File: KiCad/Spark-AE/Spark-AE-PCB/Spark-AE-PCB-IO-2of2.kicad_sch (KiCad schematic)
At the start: 42 parts, among them J7 SD_CONN, U6 MCP6002T-I_MS, U8 MCP6002T-I_MS, U9 74xGxx_MDD_74AHCT1G125GV

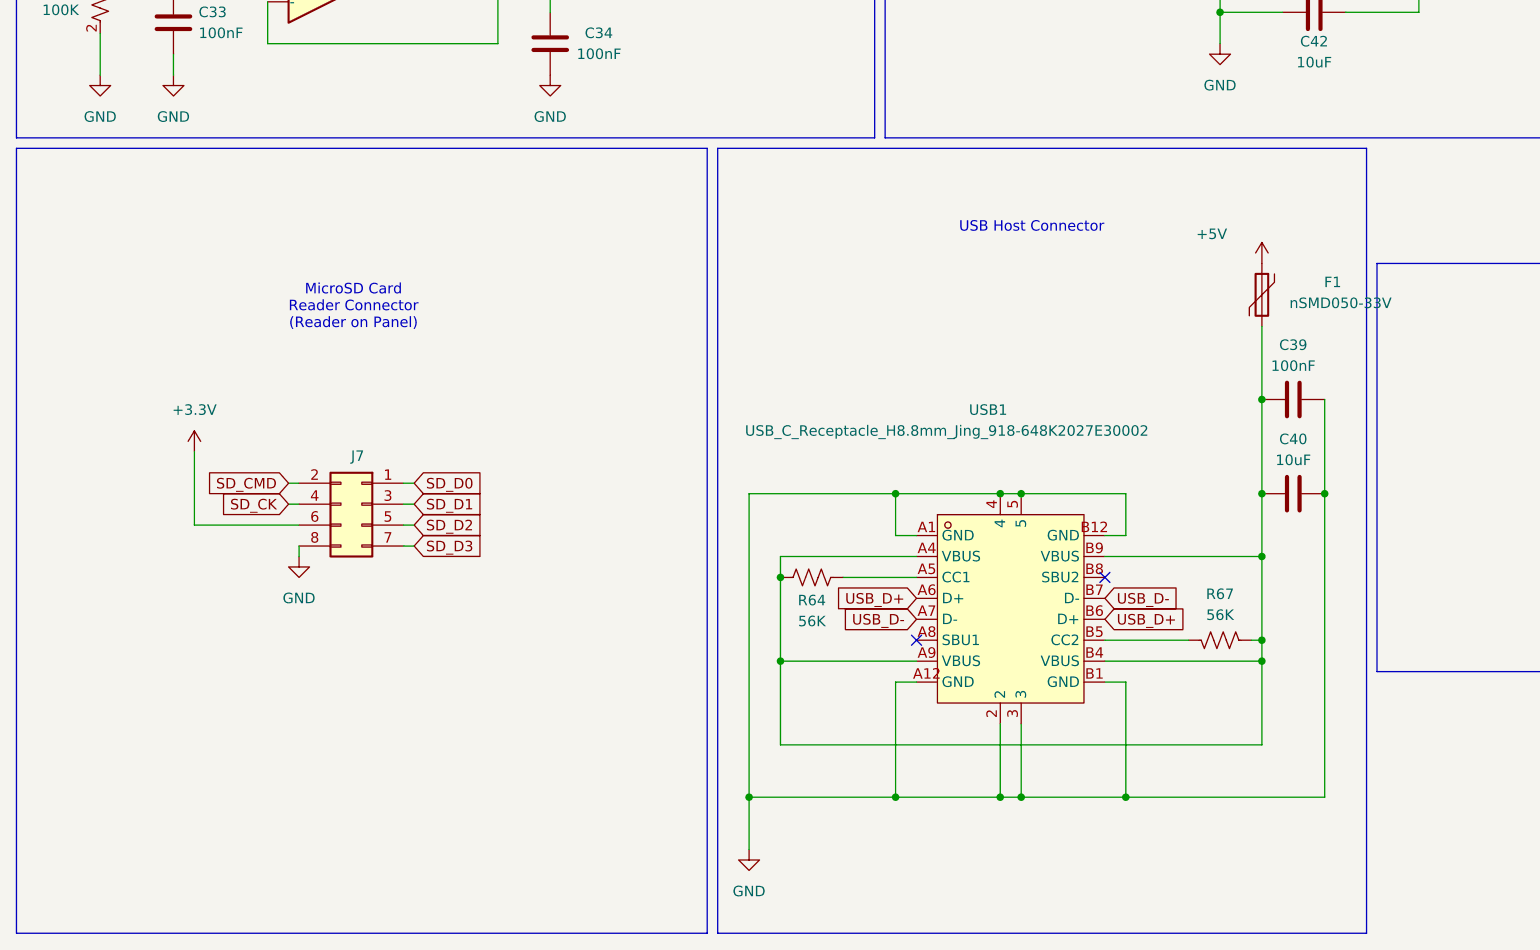
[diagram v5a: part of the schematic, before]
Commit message: mk0 prototype sent for production! commit includes a couple of necessary tweaks.
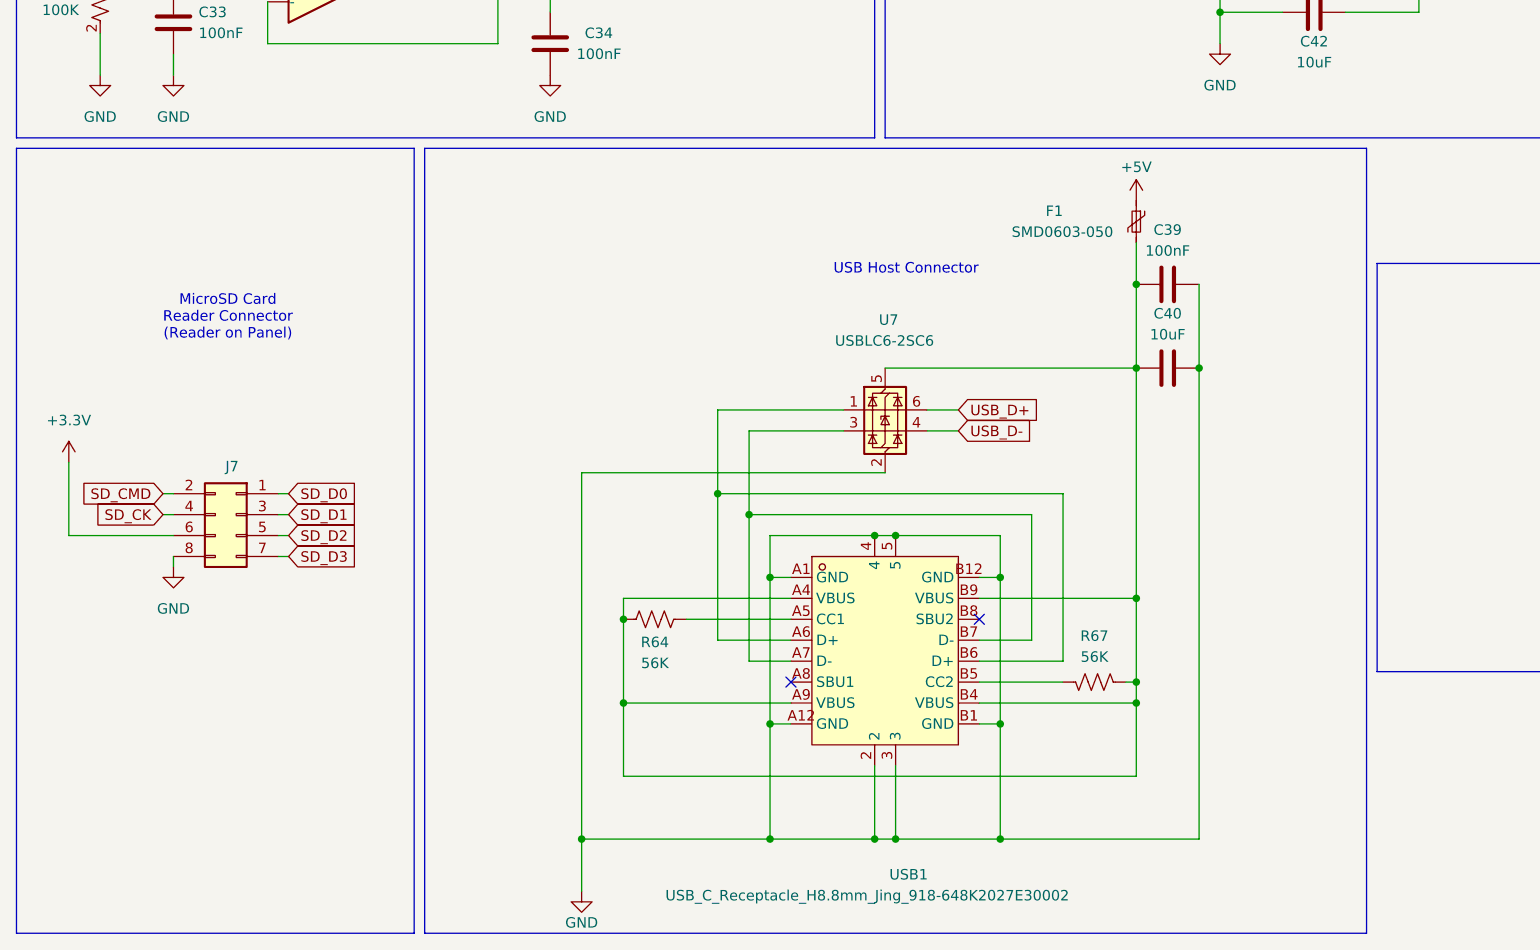
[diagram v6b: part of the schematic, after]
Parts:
- added U7: USBLC6-2SC6, Package_TO_SOT_SMD:SOT-23-6, symbol Power_Protection:USBLC6-2SC6
- F1: value nSMD050-33V -> SMD0603-050; symbol Device:Polyfuse -> Device:Polyfuse_Small
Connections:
- net GND: now also U7.2 (GND)
- net USB_D+: now also U7.6 (I/O1); no longer USB1.A6 (D+), USB1.B6 (D+)
- net USB_D-: now also U7.4 (I/O2); no longer USB1.A7 (D-), USB1.B7 (D-)
- net at C39.1, C40.1, F1.2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: now also U7.5 (VBUS)
- new net: U7.1 (I/O1), USB1.A6 (D+), USB1.B6 (D+)
- new net: U7.3 (I/O2), USB1.A7 (D-), USB1.B7 (D-)
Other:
- moved on the sheet: C39, C40, F1, J7, R64, R67, USB1
